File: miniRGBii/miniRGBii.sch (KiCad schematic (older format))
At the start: 28 parts

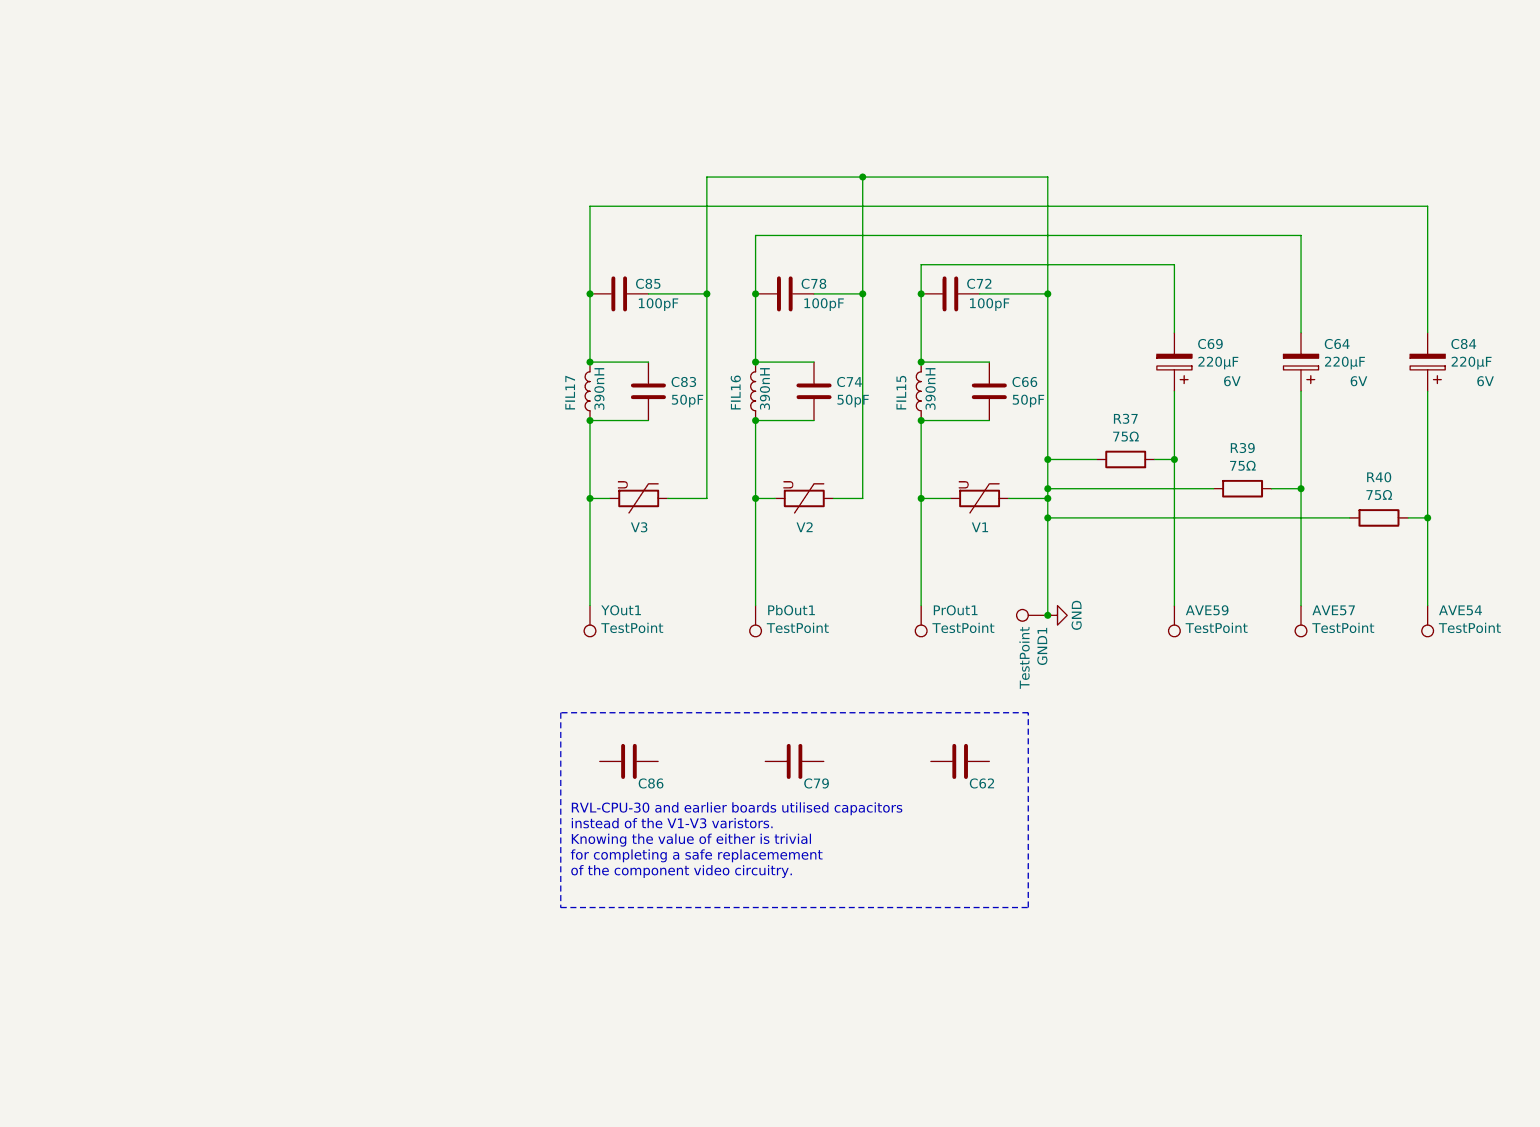
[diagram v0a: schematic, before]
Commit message: Changed schematic to look less tangled
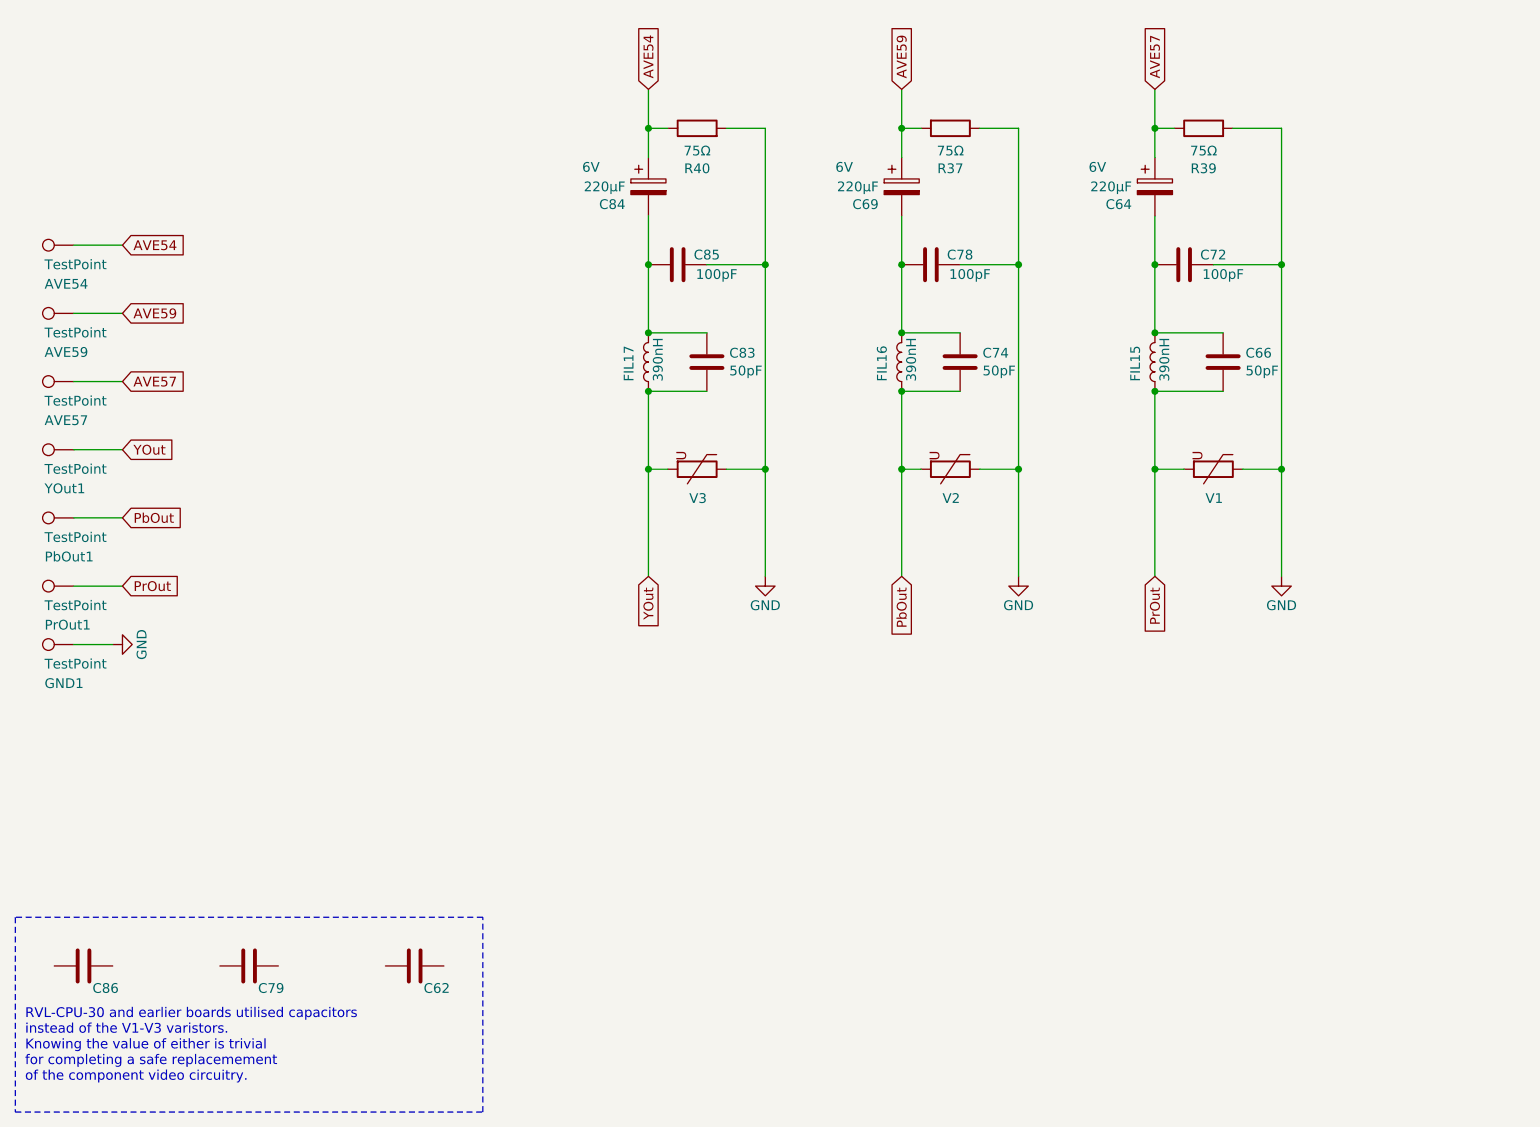
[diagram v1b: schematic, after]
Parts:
- C64, C69, C84: footprint Capacitor_SMD:CP_Elec_8x10.5 -> Capacitor_Tantalum_SMD:CP_EIA-7343-15_Kemet-W_Pad2.25x2.55mm_HandSolder
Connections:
- net PrOut: now reaches C66.2, FIL15.1, PrOut1.1, V1.2
- net at C66.1, C72.2, FIL15.2: now also C64.2; no longer C69.2
- net PbOut: now reaches C74.2, FIL16.1, PbOut1.1, V2.2
- net at C74.1, C78.2, FIL16.2: now also C69.2; no longer C64.2
- net YOut: now reaches C83.2, FIL17.1, V3.2, YOut1.1
- net AVE59: now reaches AVE59.1, C69.1, R37.2
- net AVE57: now reaches AVE57.1, C64.1, R39.1
- net AVE54: now reaches AVE54.1, C84.1, R40.1
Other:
- moved on the sheet: AVE54, AVE57, AVE59, C62, C64, C66, C69, C72, C74, C78, C79, C83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
